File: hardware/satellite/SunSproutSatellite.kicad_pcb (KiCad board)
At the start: 4 copper layers, 27.2 x 51.1 mm, 35 parts, among them J1 RJHSE5380_QwiicBusCompatible, J2 Conn_01x03, J3 Conn_01x03, J4 Conn_01x03, J5 Conn_01x03, J6 Conn_01x03, J7 Conn_01x04, U1 PCA9615DPZ, U2 ADS1115IDGS, U3 DS2482S-100+, U4 USBLC6-4SC6

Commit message: Add qwiic connection for i2c expansion. Re-render the main assets
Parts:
- added J8: Qwiic, Connector_JST:JST_SH_BM04B-SRSS-TB_1x04-1MP_P1.00mm_Vertical, F.Cu at (110.4, 114.7)
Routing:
- net SAT_3V3: track 147.6 -> 153.3 mm, vias 8 -> 9
- net GND: track 23.6 -> 27.1 mm
- net SDA_LOCAL: track 46.2 -> 48.8 mm, vias 2 -> 3
- net SCL_LOCAL: track 43.0 -> 45.0 mm, vias 3 -> 4

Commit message: Consolidate Hub and Satellite libraries into shared hardware/libraries
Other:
- board text added: "SunSproutSatellite REV ${REV_NUM}(${VCSSHORTHASH})"
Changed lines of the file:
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@@
 		(capping no)
 		(filling no)
-		(zone_defaults)
 		(pcbplotparams
 			(layerselection 0x00000000_00000000_00000000_000000a5)
@@
 		)
 	)
+	(gr_text "SunSproutSatellite\nREV ${REV_NUM}(${VCSSHORTHASH})"
+		(at 121.1 110.2 270)
+		(layer "B.SilkS")
+		(effects
+			(font
+				(size 1 1)
+			)
+			(justify mirror)
+		)
+	)
 	(gr_text "GND_1↔GND_2"
-		(at 122.7 130.1 0)
+		(at 118.4 132.9 270)
 		(layer "B.SilkS")
 		(effects
@@
 		)
 	)
+	(gr_text_box "Licensed under CERN-OHL-S v2\ngithub.com/JohnNeville/SunSprout"
+		(start 112.75 112.9)
+		(end 116.45 138.9)
+		(margins 0 0 0 0)
+		(angle 270)
+		(layer "B.SilkS")
+		(effects
+			(font
+				(size 1 0.95)
+				(thickness 0.15)
+			)
+			(justify left top mirror)
+		)
+		(border no)
+		(stroke
+			(width 0.2)
+			(type solid)
+		)
+		(knockout no)
+	)
 	(segment

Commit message: Add SunSprout logo to Satellite silkscreen and refresh documentation assets
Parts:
- added G***: LOGO, project:Logo, B.Cu at (122.1, 113.2)

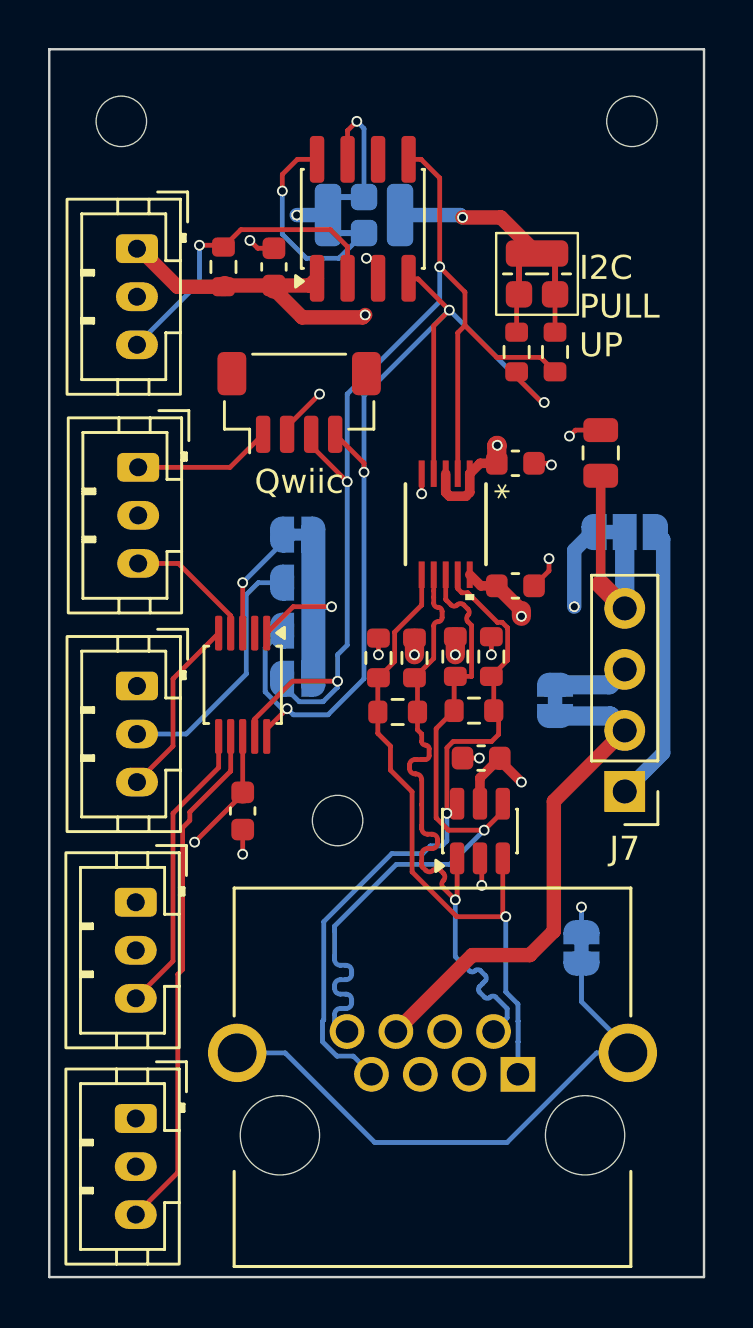
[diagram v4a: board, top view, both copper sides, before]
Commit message: feat(hardware, website): Hub & Satellite layout review fixes, interactive pinout component, and dual-board documentation (#25)
## Overview
This PR completes post-routing design review fixes across both the **SunSprout Hub** and **SunSprout Satellite** PCBs, resolves ESPHome firmware driver dependencies, and upgrades the documentation site with interactive React pinout components, enhanced typography, and a true-to-scale dual-board hero showcase.

## Key Changes

### 1. Hardware & PCB Layout Fixes
* **Checklist Audit:** Fully audited both boards against standard DFM/DFA and mass-manufacturing layout checklists (0 DRC violations, 0 unconnected items).
* **Hub Improvements (`hardware/hub`):**
  - Optimized high-current switching power loops for the BQ25798 buck-boost charger and TPS631000 3.3V rail.
  - Corrected battery fuel-gauge current-sense routing with true Kelvin connections across the sense resistor.
  - Eliminated acute trace angles and acid traps across critical signal traces.
* **Satellite Differential Routing (`hardware/satellite`):**
  - Eliminated serpentine length-tuning stubs and acute branch angles on the `DSDA_P` / `DSDA_N` differential pairs near `U1` (PCA9615).
  - Maintained continuous 100 Ω differential impedance and clean reference plane returns along Cat5/6 cable run terminations.

### 2. Firmware Updates (`firmware/`)
* **ESPHome Header Resolution:** Added a local wrapper header (`firmware/sunsprout_gpio.h`) to resolve ESPHome platform compilation issues looking for ESP-IDF's `driver/gpio.h`.
* **Action Synchronicity:** Updated external `esphome-bq-drivers` action declarations (`bq25798.clear_interrupts`, `bq34z100.clear_alert`) to declare `synchronous=True`, resolving compiler warnings and enabling ESPHome `StringRef` optimizations.
* **Sleep Leakage:** Disabled floating pull-downs and high-impedance states during deep-sleep to prevent parasitic battery drain.

### 3. Documentation Site & Interactive Pinout (`website/`, `tools/`)
* **Interacti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
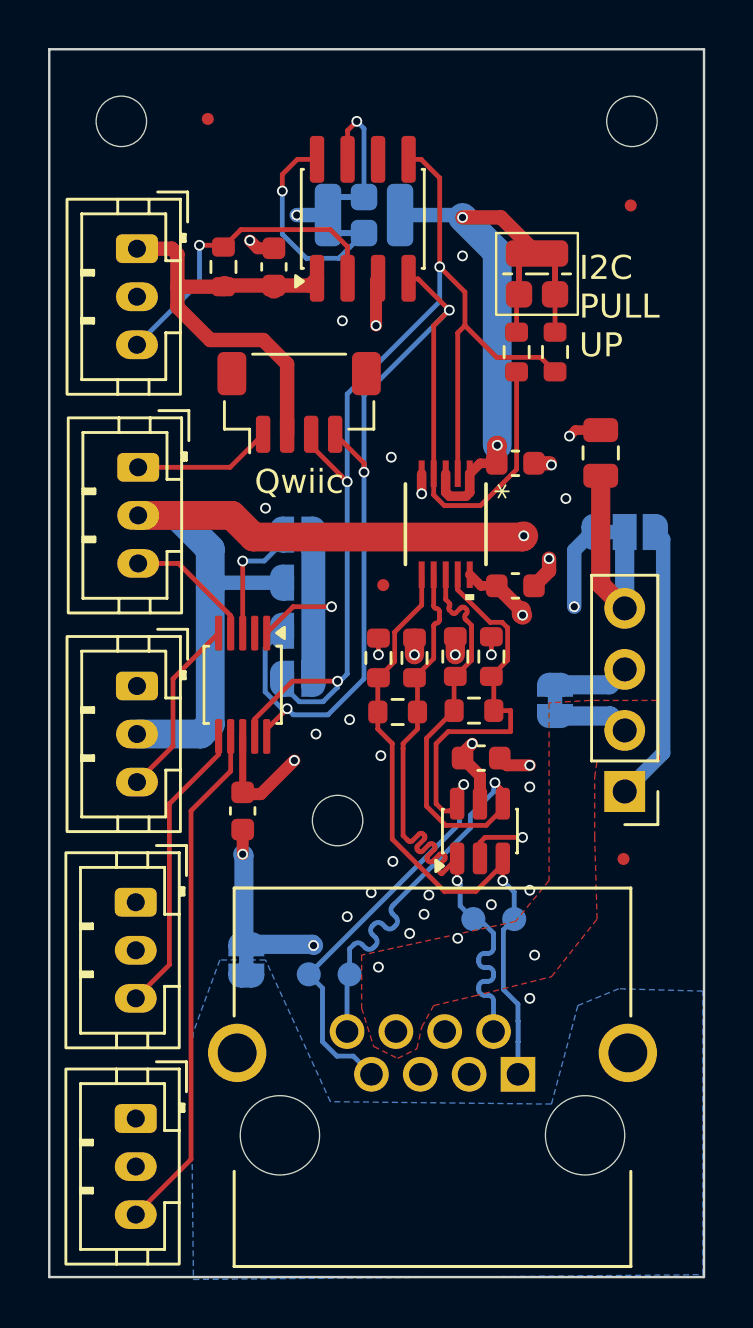
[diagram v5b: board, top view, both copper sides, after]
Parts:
- added Ref**: Fiducial_0.5mm_Mask1mm, PCM_SparkFun-Aesthetic:Fiducial_0.5mm_Mask1mm, F.Cu at (113.9, 122.3)
- added Ref**: Fiducial_0.5mm_Mask1mm, PCM_SparkFun-Aesthetic:Fiducial_0.5mm_Mask1mm, F.Cu at (106.6, 102.9)
- added Ref**: Fiducial_0.5mm_Mask1mm, PCM_SparkFun-Aesthetic:Fiducial_0.5mm_Mask1mm, F.Cu at (123.9, 133.7)
- added Ref**: Fiducial_0.5mm_Mask1mm, PCM_SparkFun-Aesthetic:Fiducial_0.5mm_Mask1mm, F.Cu at (124.2, 106.5)
- added TP4: TestPoint_2Pole, project:TestPoint_2Pole_Pad_D1.0mm, B.Cu at (118.5, 136.2)
- added TP5: TestPoint_2Pole, project:TestPoint_2Pole_Pad_D1.0mm, B.Cu at (111.7, 138.5)
- moved JP13 14.0 mm to (108.2, 137.9)
- moved G*** 3.90 mm to (122.1, 109.3)
- turned C6 to 0 degrees
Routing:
- net VCC_2: track 38.7 -> 13.2 mm
- net SHIELD: track 24.0 -> 0.00 mm
- net GND_2: track 21.0 -> 3.15 mm
- net SAT_3V3: track 153.3 -> 170.0 mm, vias 9 -> 8
- net GND: track 27.1 -> 36.6 mm, vias 14 -> 35
- net DSDA_N: track 29.2 -> 32.8 mm
- net SCL_LOCAL: track 45.0 -> 46.9 mm, vias 4 -> 3
- net DSDA_P: track 30.1 -> 31.8 mm
- net DSCL_P: track 26.8 -> 27.6 mm
- added copper zone on In2.Cu, net GND
- added copper zone on F.Cu, net GND_2
- added copper zone on B.Cu, net SHIELD
- added copper zone on In2.Cu, net VCC_2
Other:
- board text added: "+"
- board text added: "DSCL"
- board text added: "DSDA"
- board text added: "JP_VCC"
